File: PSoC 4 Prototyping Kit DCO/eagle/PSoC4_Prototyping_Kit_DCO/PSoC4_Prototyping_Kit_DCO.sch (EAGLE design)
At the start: 13 parts, among them IC1 PSOC_4_PROTOTYPING_KIT

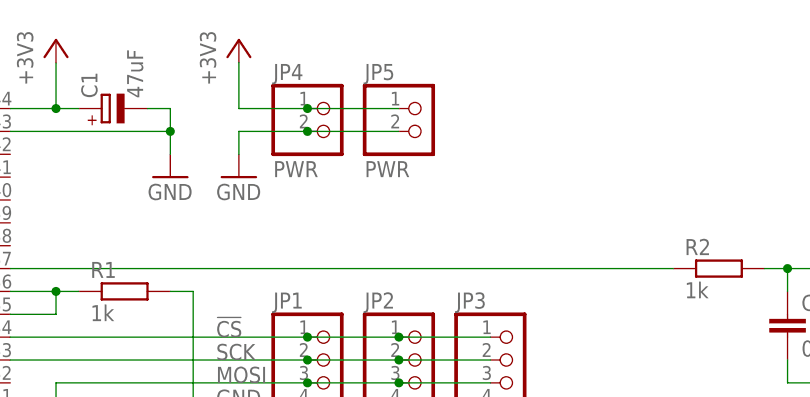
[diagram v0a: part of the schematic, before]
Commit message: Add a inverse Diode from VDD to GND
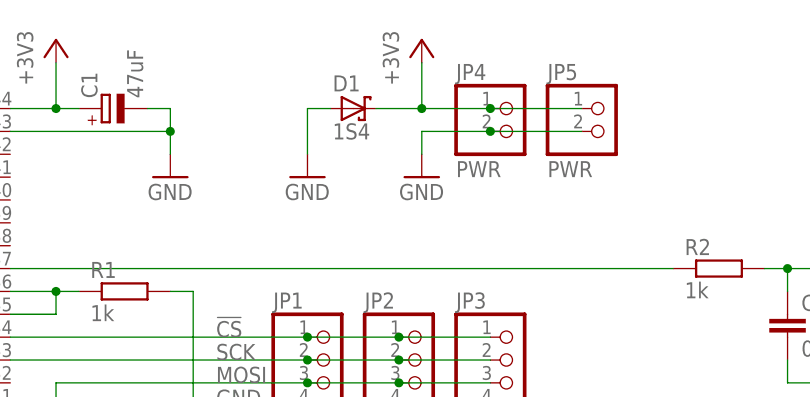
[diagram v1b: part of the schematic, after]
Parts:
- added D1: 1S4, diode:SCHOTTKY-DIODEDO35-7
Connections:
- net +3V3: now also D1.C
- net GND: now also D1.A
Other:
- moved on the sheet: JP4, JP5
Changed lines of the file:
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@@
 <setting verticaltext="up"/>
 </settings>
-<grid distance="0.1" unitdist="inch" unit="inch" style="lines" multiple="1" display="yes" altdistance="0.01" altunitdist="inch" altunit="inch"/>
+<grid distance="0.1" unitdist="inch" unit="inch" style="dots" multiple="1" display="yes" altdistance="0.01" altunitdist="inch" altunit="inch"/>
 <layers>
 <layer number="1" name="Top" color="4" fill="1" visible="no" active="no"/>
@@
 <layer number="97" name="Info" color="7" fill="1" visible="yes" active="yes"/>
 <layer number="98" name="Guide" color="6" fill="1" visible="yes" active="yes"/>
+<layer number="99" name="SpiceOrder" color="5" fill="1" visible="yes" active="yes"/>
 <layer number="200" name="200bmp" color="1" fill="10" visible="no" active="no"/>
 <layer number="201" name="tNamesOnPCB" color="5" fill="1" visible="yes" active="yes"/>
@@
 <part name="JP5" library="pinhead" deviceset="PINHD-1X2" device="" value="PWR"/>
 <part name="JP2" library="pinhead" deviceset="PINHD-1X4" device="" value="SPI"/>
+<part name="D1" library="diode" deviceset="SCHOTTKY-DIODE" device="DO35-7" value="1S4"/>
+<part name="GND6" library="supply1" deviceset="GND" device=""/>
 </parts>
 <sheets>
@@
 <instance part="JK1" gate="G$1" x="200.66" y="96.52"/>
 <instance part="GND3" gate="1" x="198.12" y="73.66"/>
-<instance part="JP4" gate="G$1" x="137.16" y="111.76"/>
-<instance part="+3V2" gate="G$1" x="127" y="121.92"/>
-<instance part="GND4" gate="1" x="127" y="106.68"/>
+<instance part="JP4" gate="G$1" x="157.48" y="111.76"/>
+<instance part="+3V2" gate="G$1" x="147.32" y="121.92"/>
+<instance part="GND4" gate="1" x="147.32" y="106.68"/>
 <instance part="R2" gate="G$1" x="180.34" y="96.52"/>
 <instance part="C2" gate="G$1" x="187.96" y="91.44"/>
@@
 <instance part="+3V3" gate="G$1" x="71.12" y="121.92"/>
 <instance part="JP3" gate="A" x="157.48" y="83.82"/>
-<instance part="JP5" gate="G$1" x="147.32" y="111.76"/>
+<instance part="JP5" gate="G$1" x="167.64" y="111.76"/>
 <instance part="JP2" gate="A" x="147.32" y="83.82"/>
+<instance part="D1" gate="G$1" x="139.7" y="114.3"/>
+<instance part="GND6" gate="1" x="134.62" y="106.68"/>
 </instances>
 <busses>
@@
 <segment>
 <pinref part="+3V2" gate="G$1" pin="+3V3"/>
-<wire x1="127" y1="119.38" x2="127" y2="114.3" width="0.1524" layer="91"/>
+<wire x1="147.32" y1="119.38" x2="147.32" y2="114.3" width="0.1524" layer="91"/>
 <pinref part="JP4" gate="G$1" pin="1"/>
-<wire x1="127" y1="114.3" x2="134.62" y2="114.3" width="0.1524" layer="91"/>
-<wire x1="134.62" y1="114.3" x2="144.78" y2="114.3" width="0.1524" layer="91"/>
-<junction x="134.62" y="114.3"/>
+<wire x1="147.32" y1="114.3" x2="154.94" y2="114.3" width="0.1524" layer="91"/>
+<wire x1="154.94" y1="114.3" x2="165.1" y2="114.3" width="0.1524" layer="91"/>
+<junction x="154.94" y="114.3"/>
 <pinref part="JP5" gate="G$1" pin="1"/>
+<pinref part="D1" gate="G$1" pin="C"/>
+<wire x1="142.24" y1="114.3" x2="147.32" y2="114.3" width="0.1524" layer="91"/>
+<junction x="147.32" y="114.3"/>
 </segment>
 <segment>
@@
 <segment>
 <pinref part="GND4" gate="1" pin="GND"/>
-<wire x1="127" y1="109.22" x2="127" y2="111.76" width="0.1524" layer="91"/>
+<wire x1="147.32" y1="109.22" x2="147.32" y2="111.76" width="0.1524" layer="91"/>
 <pinref part="JP4" gate="G$1" pin="2"/>
-<wire x1="127" y1="111.76" x2="134.62" y2="111.76" width="0.1524" layer="91"/>
+<wire x1="147.32" y1="111.76" x2="154.94" y2="111.76" width="0.1524" layer="91"/>
 <pinref part="JP5" gate="G$1" pin="2"/>
-<wire x1="134.62" y1="111.76" x2="144.78" y2="111.76" width="0.1524" layer="91"/>
-<junction x="134.62" y="111.76"/>
+<wire x1="154.94" y1="111.76" x2="165.1" y2="111.76" width="0.1524" layer="91"/>
+<junction x="154.94" y="111.76"/>
 </segment>
 <segment>
@@
 <wire x1="71.12" y1="96.52" x2="71.12" y2="93.98" width="0.1524" layer="91"/>
 </segment>
+<segment>
+<pinref part="GND6" gate="1" pin="GND"/>
+<wire x1="134.62" y1="109.22" x2="134.62" y2="114.3" width="0.1524" layer="91"/>
+<pinref part="D1" gate="G$1" pin="A"/>
+<wire x1="134.62" y1="114.3" x2="137.16" y2="114.3" width="0.1524" layer="91"/>
+</segment>
 </net>

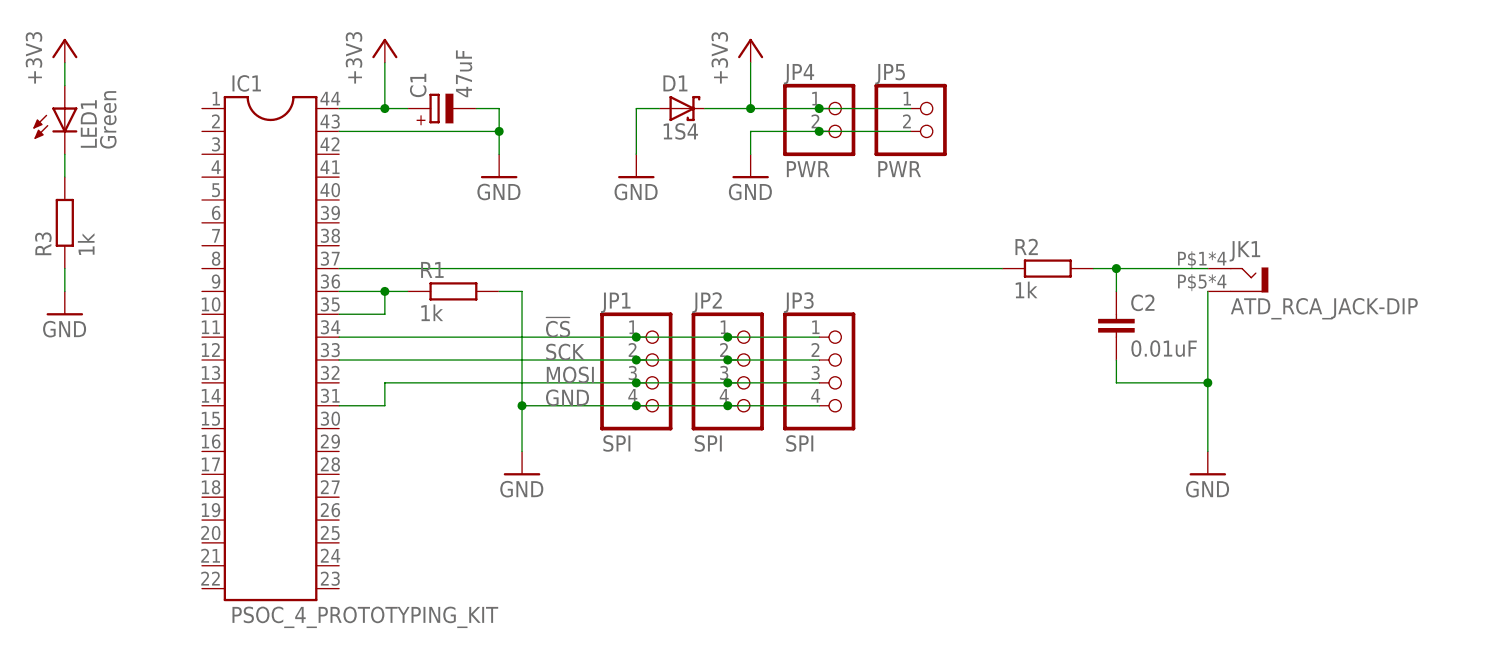
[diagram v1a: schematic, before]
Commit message: Add: Reset Line
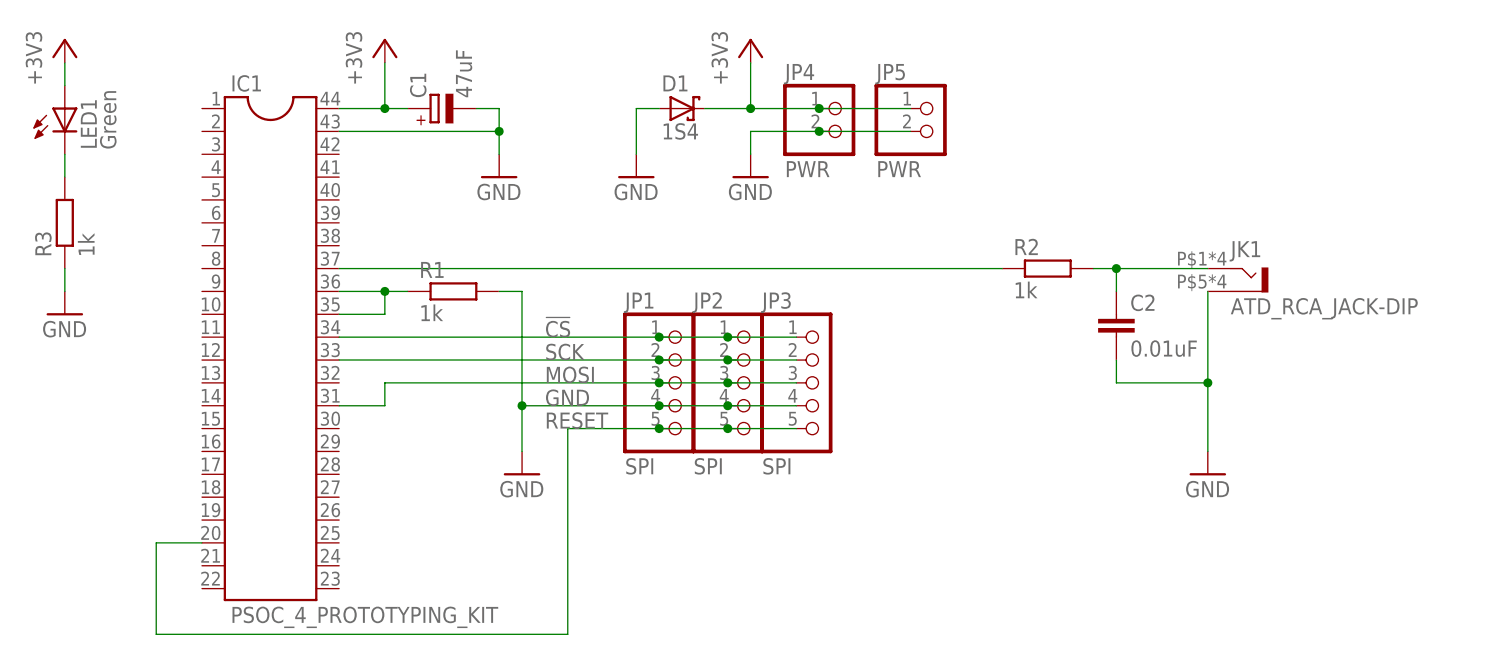
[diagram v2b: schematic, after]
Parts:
- JP1, JP2, JP3: device pinhead:PINHD-1X4 -> pinhead:PINHD-1X5
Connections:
- new net RESET: IC1.20, JP1.5, JP2.5, JP3.5
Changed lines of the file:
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@@
 <setting verticaltext="up"/>
 </settings>
-<grid distance="0.1" unitdist="inch" unit="inch" style="dots" multiple="1" display="yes" altdistance="0.01" altunitdist="inch" altunit="inch"/>
+<grid distance="0.1" unitdist="inch" unit="inch" style="lines" multiple="1" display="no" altdistance="0.01" altunitdist="inch" altunit="inch"/>
 <layers>
 <layer number="1" name="Top" color="4" fill="1" visible="no" active="no"/>
@@
 <part name="R2" library="rcl" deviceset="R-EU_" device="0207/7" value="1k"/>
 <part name="C2" library="rcl" deviceset="C-EU" device="050-024X044" value="0.01uF"/>
-<part name="JP1" library="pinhead" deviceset="PINHD-1X4" device="" value="SPI"/>
 <part name="FRAME1" library="frames" deviceset="A4L-LOC" device="" value="Frame"/>
 <part name="LED1" library="led" deviceset="LED" device="3MM" value="Green"/>
@@
 <part name="GND5" library="supply1" deviceset="GND" device=""/>
 <part name="+3V3" library="supply1" deviceset="+3V3" device=""/>
-<part name="JP3" library="pinhead" deviceset="PINHD-1X4" device="" value="SPI"/>
 <part name="JP5" library="pinhead" deviceset="PINHD-1X2" device="" value="PWR"/>
-<part name="JP2" library="pinhead" deviceset="PINHD-1X4" device="" value="SPI"/>
 <part name="D1" library="diode" deviceset="SCHOTTKY-DIODE" device="DO35-7" value="1S4"/>
 <part name="GND6" library="supply1" deviceset="GND" device=""/>
+<part name="JP1" library="pinhead" deviceset="PINHD-1X5" device="" value="SPI"/>
+<part name="JP2" library="pinhead" deviceset="PINHD-1X5" device="" value="SPI"/>
+<part name="JP3" library="pinhead" deviceset="PINHD-1X5" device="" value="SPI"/>
 </parts>
 <sheets>
@@
 <instance part="R2" gate="G$1" x="180.34" y="96.52"/>
 <instance part="C2" gate="G$1" x="187.96" y="91.44"/>
-<instance part="JP1" gate="A" x="137.16" y="83.82"/>
 <instance part="FRAME1" gate="G$1" x="0" y="0"/>
 <instance part="LED1" gate="G$1" x="71.12" y="114.3"/>
@@
 <instance part="GND5" gate="1" x="71.12" y="91.44"/>
 <instance part="+3V3" gate="G$1" x="71.12" y="121.92"/>
-<instance part="JP3" gate="A" x="157.48" y="83.82"/>
 <instance part="JP5" gate="G$1" x="167.64" y="111.76"/>
-<instance part="JP2" gate="A" x="147.32" y="83.82"/>
 <instance part="D1" gate="G$1" x="139.7" y="114.3"/>
 <instance part="GND6" gate="1" x="134.62" y="106.68"/>
+<instance part="JP1" gate="A" x="139.7" y="83.82"/>
+<instance part="JP2" gate="A" x="147.32" y="83.82"/>
+<instance part="JP3" gate="A" x="154.94" y="83.82"/>
 </instances>
 <busses>
@@
 <pinref part="GND2" gate="1" pin="GND"/>
 <wire x1="121.92" y1="81.28" x2="121.92" y2="76.2" width="0.1524" layer="91"/>
-<wire x1="134.62" y1="81.28" x2="121.92" y2="81.28" width="0.1524" layer="91"/>
 <junction x="121.92" y="81.28"/>
+<label x="124.46" y="81.28" size="1.778" layer="95"/>
 <pinref part="JP1" gate="A" pin="4"/>
-<label x="124.46" y="81.28" size="1.778" layer="95"/>
-<junction x="134.62" y="81.28"/>
+<wire x1="152.4" y1="81.28" x2="144.78" y2="81.28" width="0.1524" layer="91"/>
+<wire x1="144.78" y1="81.28" x2="137.16" y2="81.28" width="0.1524" layer="91"/>
+<wire x1="137.16" y1="81.28" x2="121.92" y2="81.28" width="0.1524" layer="91"/>
+<junction x="137.16" y="81.28"/>
+<pinref part="JP2" gate="A" pin="4"/>
+<junction x="144.78" y="81.28"/>
 <pinref part="JP3" gate="A" pin="4"/>
-<wire x1="134.62" y1="81.28" x2="144.78" y2="81.28" width="0.1524" layer="91"/>
-<pinref part="JP2" gate="A" pin="4"/>
-<wire x1="144.78" y1="81.28" x2="154.94" y2="81.28" width="0.1524" layer="91"/>
-<junction x="144.78" y="81.28"/>
 </segment>
 <segment>
@@
 <pinref part="IC1" gate="G$1" pin="31"/>
 <wire x1="101.6" y1="81.28" x2="106.68" y2="81.28" width="0.1524" layer="91"/>
-<wire x1="134.62" y1="83.82" x2="106.68" y2="83.82" width="0.1524" layer="91"/>
+<wire x1="152.4" y1="83.82" x2="144.78" y2="83.82" width="0.1524" layer="91"/>
+<wire x1="144.78" y1="83.82" x2="137.16" y2="83.82" width="0.1524" layer="91"/>
+<wire x1="137.16" y1="83.82" x2="106.68" y2="83.82" width="0.1524" layer="91"/>
 <wire x1="106.68" y1="83.82" x2="106.68" y2="81.28" width="0.1524" layer="91"/>
 <label x="124.46" y="83.82" size="1.778" layer="95"/>
 <pinref part="JP1" gate="A" pin="3"/>
-<junction x="134.62" y="83.82"/>
+<junction x="137.16" y="83.82"/>
+<pinref part="JP2" gate="A" pin="3"/>
+<junction x="144.78" y="83.82"/>
 <pinref part="JP3" gate="A" pin="3"/>
-<wire x1="134.62" y1="83.82" x2="144.78" y2="83.82" width="0.1524" layer="91"/>
-<pinref part="JP2" gate="A" pin="3"/>
-<wire x1="144.78" y1="83.82" x2="154.94" y2="83.82" width="0.1524" layer="91"/>
-<junction x="144.78" y="83.82"/>
 </segment>
 </net>
@@
 <segment>
 <pinref part="IC1" gate="G$1" pin="33"/>
-<wire x1="101.6" y1="86.36" x2="134.62" y2="86.36" width="0.1524" layer="91"/>
+<wire x1="101.6" y1="86.36" x2="137.16" y2="86.36" width="0.1524" layer="91"/>
 <label x="124.46" y="86.36" size="1.778" layer="95"/>
 <pinref part="JP1" gate="A" pin="2"/>
-<junction x="134.62" y="86.36"/>
+<wire x1="137.16" y1="86.36" x2="144.78" y2="86.36" width="0.1524" layer="91"/>
+<junction x="137.16" y="86.36"/>
+<pinref part="JP2" gate="A" pin="2"/>
+<wire x1="144.78" y1="86.36" x2="152.4" y2="86.36" width="0.1524" layer="91"/>
+<junction x="144.78" y="86.36"/>
 <pinref part="JP3" gate="A" pin="2"/>
-<wire x1="134.62" y1="86.36" x2="144.78" y2="86.36" width="0.1524" layer="91"/>
-<pinref part="JP2" gate="A" pin="2"/>
-<wire x1="144.78" y1="86.36" x2="154.94" y2="86.36" width="0.1524" layer="91"/>
-<junction x="144.78" y="86.36"/>
 </segment>
 </net>
@@
 <segment>
 <pinref part="IC1" gate="G$1" pin="34"/>
-<wire x1="101.6" y1="88.9" x2="134.62" y2="88.9" width="0.1524" layer="91"/>
+<wire x1="101.6" y1="88.9" x2="137.16" y2="88.9" width="0.1524" layer="91"/>
 <label x="124.46" y="88.9" size="1.778" layer="95"/>
 <pinref part="JP1" gate="A" pin="1"/>
+<wire x1="137.16" y1="88.9" x2="144.78" y2="88.9" width="0.1524" layer="91"/>
+<junction x="137.16" y="88.9"/>
 <pinref part="JP2" gate="A" pin="1"/>
-<wire x1="134.62" y1="88.9" x2="144.78" y2="88.9" width="0.1524" layer="91"/>
-<junction x="134.62" y="88.9"/>
+<wire x1="144.78" y1="88.9" x2="152.4" y2="88.9" width="0.1524" layer="91"/>
+<junction x="144.78" y="88.9"/>
 <pinref part="JP3" gate="A" pin="1"/>
-<wire x1="144.78" y1="88.9" x2="154.94" y2="88.9" width="0.1524" layer="91"/>
-<junction x="144.78" y="88.9"/>
 </segment>
 </net>
@@
 </segment>
 </net>
+<net name="RESET" class="0">
+<segment>
+<pinref part="IC1" gate="G$1" pin="20"/>
+<wire x1="86.36" y1="66.04" x2="81.28" y2="66.04" width="0.1524" layer="91"/>
+<wire x1="81.28" y1="66.04" x2="81.28" y2="55.88" width="0.1524" layer="91"/>
+<wire x1="81.28" y1="55.88" x2="127" y2="55.88" width="0.1524" layer="91"/>
+<wire x1="127" y1="55.88" x2="127" y2="78.74" width="0.1524" layer="91"/>
+<pinref part="JP1" gate="A" pin="5"/>
+<wire x1="127" y1="78.74" x2="137.16" y2="78.74" width="0.1524" layer="91"/>
+<pinref part="JP2" gate="A" pin="5"/>
+<wire x1="137.16" y1="78.74" x2="144.78" y2="78.74" width="0.1524" layer="91"/>
+<junction x="137.16" y="78.74"/>
+<pinref part="JP3" gate="A" pin="5"/>
+<wire x1="144.78" y1="78.74" x2="152.4" y2="78.74" width="0.1524" layer="91"/>
+<junction x="144.78" y="78.74"/>
+<label x="124.46" y="78.74" size="1.778" layer="95"/>
+</segment>
+</net>
